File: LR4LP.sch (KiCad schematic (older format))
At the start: 13 parts, among them U2 NE5532

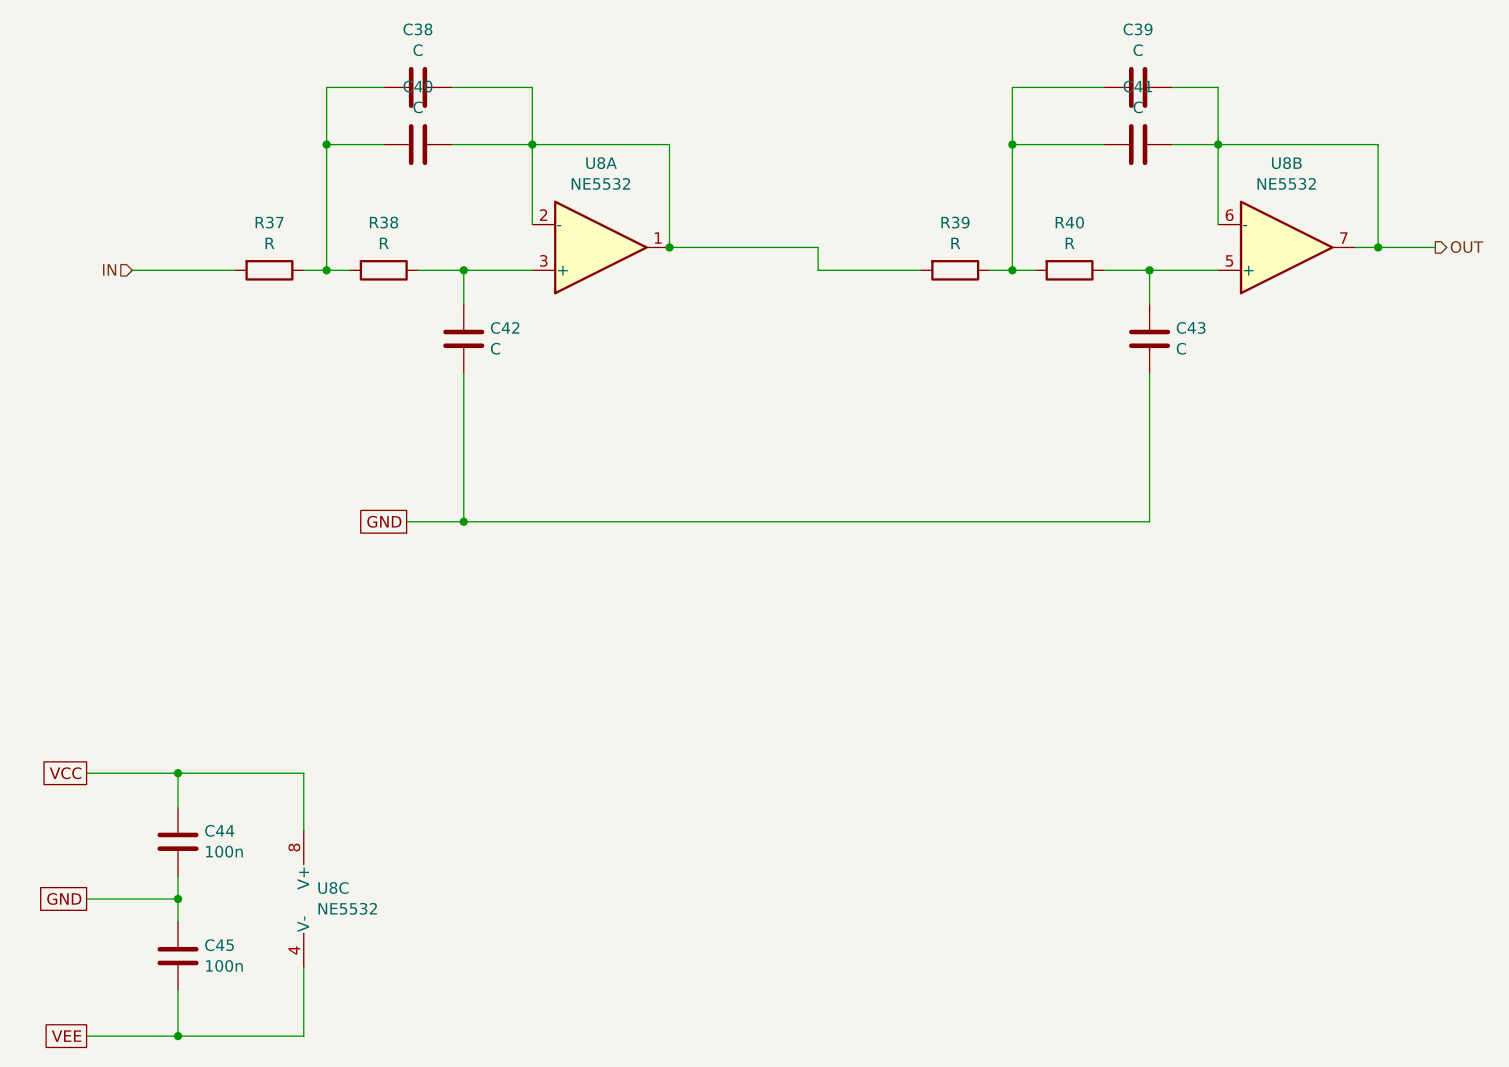
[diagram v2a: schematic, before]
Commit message: inverted LF processing chain, now with BW2 subsonic filter
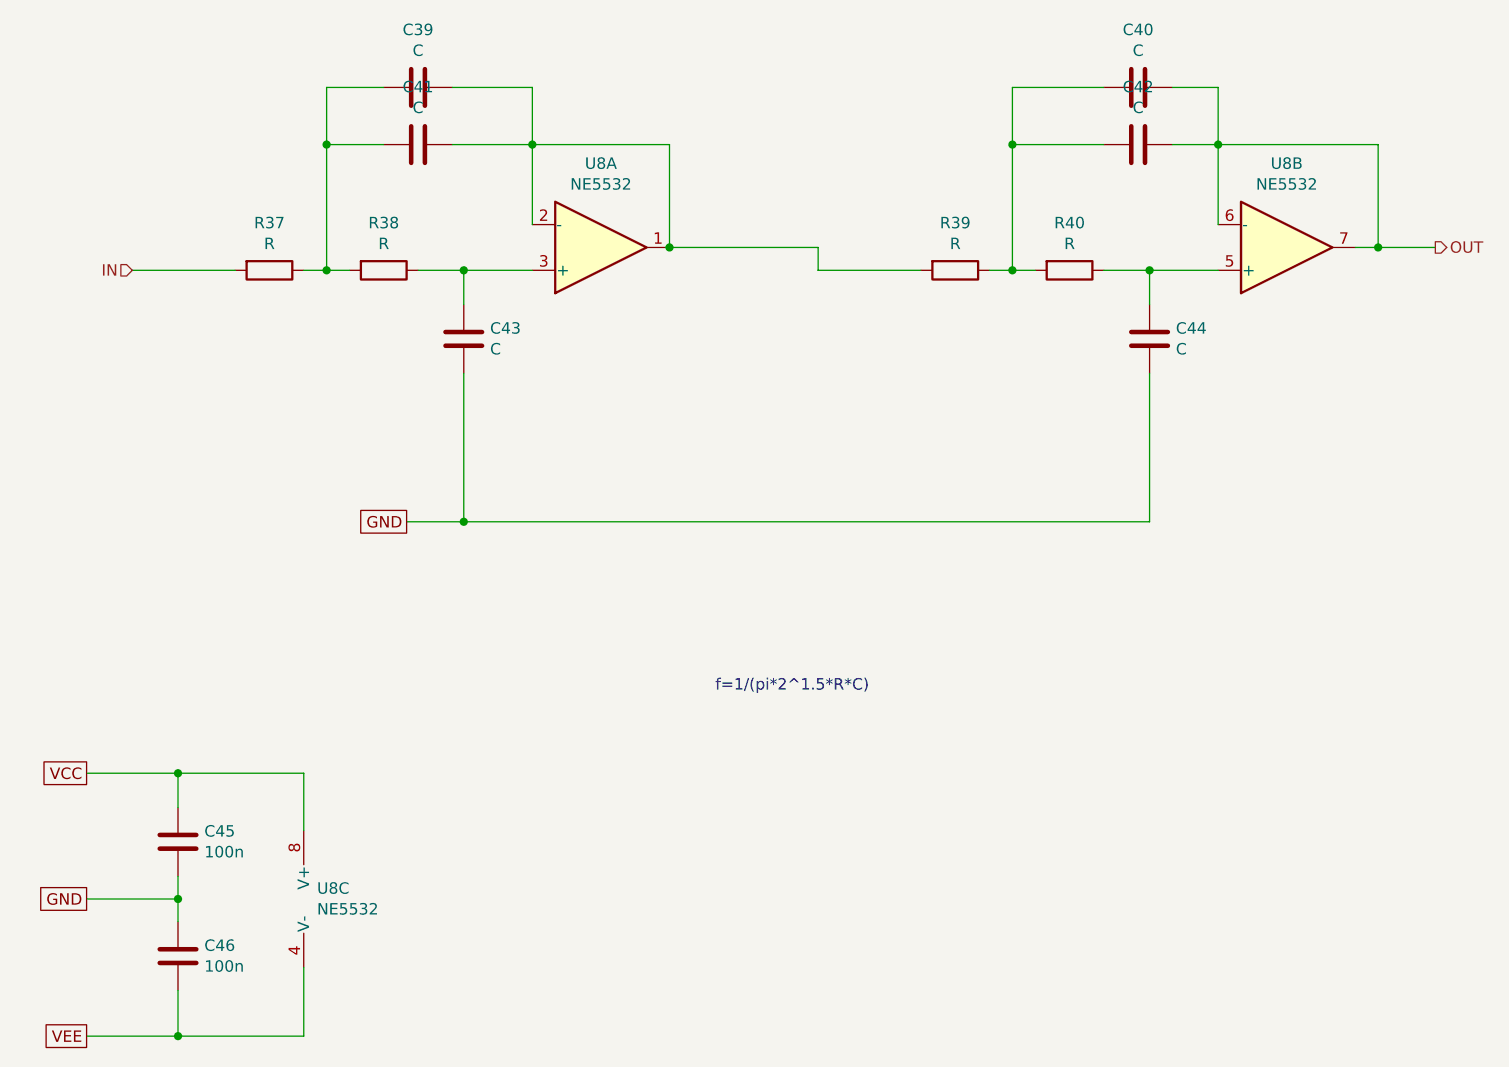
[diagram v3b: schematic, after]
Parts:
- renumbered C9 to C10, C10 to C11, C11 to C12, C4 to C5, C5 to C6, C6 to C7, C7 to C8, C8 to C9
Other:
- note added: "f=1/(pi*2^1.5*R*C)"
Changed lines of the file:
@@
 $Descr A4 11693 8268
 encoding utf-8
-Sheet 7 19
+Sheet 7 17
 Title "4th Order Linkwitz-Riley Low-Pass"
 Date "2021-10-03"
@@
 P 3000 5450
 AR Path="/6157B871/615EA97C" Ref="C?"  Part="1"
-AR Path="/615E7263/615EA97C" Ref="C11"  Part="1"
-AR Path="/615961F5/615EA97C" Ref="C25"  Part="1"
+AR Path="/615E7263/615EA97C" Ref="C12"  Part="1"
+AR Path="/615961F5/615EA97C" Ref="C26"  Part="1"
 AR Path="/61596D2E/615EA97C" Ref="C?"  Part="1"
 AR Path="/61597705/615EA97C" Ref="C?"  Part="1"
-AR Path="/615C4B58/615EA97C" Ref="C45"  Part="1"
-F 0 "C45" H 3115 5496 50  0000 L CNN
+AR Path="/615C4B58/615EA97C" Ref="C46"  Part="1"
+F 0 "C46" H 3115 5496 50  0000 L CNN
 F 1 "100n" H 3115 5405 50  0000 L CNN
 F 2 "Capacitors_SMD:C_0805" H 3038 5300 50  0001 C CNN
@@
 P 4050 1900
 AR Path="/6157B871/615EA9A2" Ref="C?"  Part="1"
-AR Path="/615E7263/615EA9A2" Ref="C6"  Part="1"
-AR Path="/615961F5/615EA9A2" Ref="C20"  Part="1"
+AR Path="/615E7263/615EA9A2" Ref="C7"  Part="1"
+AR Path="/615961F5/615EA9A2" Ref="C21"  Part="1"
 AR Path="/61596D2E/615EA9A2" Ref="C?"  Part="1"
 AR Path="/61597705/615EA9A2" Ref="C?"  Part="1"
-AR Path="/615C4B58/615EA9A2" Ref="C40"  Part="1"
-F 0 "C40" V 3798 1900 50  0000 C CNN
+AR Path="/615C4B58/615EA9A2" Ref="C41"  Part="1"
+F 0 "C41" V 3798 1900 50  0000 C CNN
 F 1 "C" V 3889 1900 50  0000 C CNN
 F 2 "Capacitors_SMD:C_1210_HandSoldering" H 4088 1750 50  0001 C CNN
@@
 P 4250 2750
 AR Path="/6157B871/615EA9A8" Ref="C?"  Part="1"
-AR Path="/615E7263/615EA9A8" Ref="C8"  Part="1"
-AR Path="/615961F5/615EA9A8" Ref="C22"  Part="1"
+AR Path="/615E7263/615EA9A8" Ref="C9"  Part="1"
+AR Path="/615961F5/615EA9A8" Ref="C23"  Part="1"
 AR Path="/61596D2E/615EA9A8" Ref="C?"  Part="1"
 AR Path="/61597705/615EA9A8" Ref="C?"  Part="1"
-AR Path="/615C4B58/615EA9A8" Ref="C42"  Part="1"
-F 0 "C42" H 4135 2704 50  0000 R CNN
+AR Path="/615C4B58/615EA9A8" Ref="C43"  Part="1"
+F 0 "C43" H 4135 2704 50  0000 R CNN
 F 1 "C" H 4135 2795 50  0000 R CNN
 F 2 "Capacitors_SMD:C_1210_HandSoldering" H 4288 2600 50  0001 C CNN
@@
 P 3000 4950
 AR Path="/6157B871/615EA9EC" Ref="C?"  Part="1"
-AR Path="/615E7263/615EA9EC" Ref="C10"  Part="1"
-AR Path="/615961F5/615EA9EC" Ref="C24"  Part="1"
+AR Path="/615E7263/615EA9EC" Ref="C11"  Part="1"
+AR Path="/615961F5/615EA9EC" Ref="C25"  Part="1"
 AR Path="/61596D2E/615EA9EC" Ref="C?"  Part="1"
 AR Path="/61597705/615EA9EC" Ref="C?"  Part="1"
-AR Path="/615C4B58/615EA9EC" Ref="C44"  Part="1"
-F 0 "C44" H 3115 4996 50  0000 L CNN
+AR Path="/615C4B58/615EA9EC" Ref="C45"  Part="1"
+F 0 "C45" H 3115 4996 50  0000 L CNN
 F 1 "100n" H 3115 4905 50  0000 L CNN
 F 2 "Capacitors_SMD:C_0805" H 3038 4800 50  0001 C CNN
@@
 P 4050 1650
 AR Path="/6157B871/6160176B" Ref="C?"  Part="1"
-AR Path="/615E7263/6160176B" Ref="C4"  Part="1"
-AR Path="/615961F5/6160176B" Ref="C18"  Part="1"
+AR Path="/615E7263/6160176B" Ref="C5"  Part="1"
+AR Path="/615961F5/6160176B" Ref="C19"  Part="1"
 AR Path="/61596D2E/6160176B" Ref="C?"  Part="1"
 AR Path="/61597705/6160176B" Ref="C?"  Part="1"
-AR Path="/615C4B58/6160176B" Ref="C38"  Part="1"
-F 0 "C38" V 3798 1650 50  0000 C CNN
+AR Path="/615C4B58/6160176B" Ref="C39"  Part="1"
+F 0 "C39" V 3798 1650 50  0000 C CNN
 F 1 "C" V 3889 1650 50  0000 C CNN
 F 2 "Capacitors_SMD:C_1210_HandSoldering" H 4088 1500 50  0001 C CNN
@@
 P 7200 1900
 AR Path="/6157B871/61611E78" Ref="C?"  Part="1"
-AR Path="/615E7263/61611E78" Ref="C7"  Part="1"
-AR Path="/615961F5/61611E78" Ref="C21"  Part="1"
+AR Path="/615E7263/61611E78" Ref="C8"  Part="1"
+AR Path="/615961F5/61611E78" Ref="C22"  Part="1"
 AR Path="/61596D2E/61611E78" Ref="C?"  Part="1"
 AR Path="/61597705/61611E78" Ref="C?"  Part="1"
-AR Path="/615C4B58/61611E78" Ref="C41"  Part="1"
-F 0 "C41" V 6948 1900 50  0000 C CNN
+AR Path="/615C4B58/61611E78" Ref="C42"  Part="1"
+F 0 "C42" V 6948 1900 50  0000 C CNN
 F 1 "C" V 7039 1900 50  0000 C CNN
 F 2 "Capacitors_SMD:C_1210_HandSoldering" H 7238 1750 50  0001 C CNN
@@
 P 7250 2750
 AR Path="/6157B871/61611E7E" Ref="C?"  Part="1"
-AR Path="/615E7263/61611E7E" Ref="C9"  Part="1"
-AR Path="/615961F5/61611E7E" Ref="C23"  Part="1"
+AR Path="/615E7263/61611E7E" Ref="C10"  Part="1"
+AR Path="/615961F5/61611E7E" Ref="C24"  Part="1"
 AR Path="/61596D2E/61611E7E" Ref="C?"  Part="1"
 AR Path="/61597705/61611E7E" Ref="C?"  Part="1"
-AR Path="/615C4B58/61611E7E" Ref="C43"  Part="1"
-F 0 "C43" H 7135 2704 50  0000 R CNN
+AR Path="/615C4B58/61611E7E" Ref="C44"  Part="1"
+F 0 "C44" H 7135 2704 50  0000 R CNN
 F 1 "C" H 7135 2795 50  0000 R CNN
 F 2 "Capacitors_SMD:C_1210_HandSoldering" H 7288 2600 50  0001 C CNN
@@
 P 7200 1650
 AR Path="/6157B871/61611E88" Ref="C?"  Part="1"
-AR Path="/615E7263/61611E88" Ref="C5"  Part="1"
-AR Path="/615961F5/61611E88" Ref="C19"  Part="1"
+AR Path="/615E7263/61611E88" Ref="C6"  Part="1"
+AR Path="/615961F5/61611E88" Ref="C20"  Part="1"
 AR Path="/61596D2E/61611E88" Ref="C?"  Part="1"
 AR Path="/61597705/61611E88" Ref="C?"  Part="1"
-AR Path="/615C4B58/61611E88" Ref="C39"  Part="1"
-F 0 "C39" V 6948 1650 50  0000 C CNN
+AR Path="/615C4B58/61611E88" Ref="C40"  Part="1"
+F 0 "C40" V 6948 1650 50  0000 C CNN
 F 1 "C" V 7039 1650 50  0000 C CNN
 F 2 "Capacitors_SMD:C_1210_HandSoldering" H 7238 1500 50  0001 C CNN
@@
 Wire Wire Line
 	8250 2350 8500 2350
+Text Notes 5350 4300 0    50   ~ 0
+f=1/(pi*2^1.5*R*C)
 $EndSCHEMATC

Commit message: Board is placed and about half-routed
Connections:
- net VP1: now reaches C9.2, R6.1, U2.3 (+)
- net FB1: now reaches C5.1, C7.1, R7.2, U2.1, U2.2 (-)
- net VP2: now reaches C10.2, R8.1, U2.5 (+)
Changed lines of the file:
@@
 $Descr A4 11693 8268
 encoding utf-8
-Sheet 7 17
+Sheet 4 17
 Title "4th Order Linkwitz-Riley Low-Pass"
 Date "2021-10-03"
@@
 Wire Wire Line
 	8250 2350 8500 2350
-Text Notes 5350 4300 0    50   ~ 0
+Text Notes 5400 3000 0    50   ~ 0
 f=1/(pi*2^1.5*R*C)
+Text Label 3000 2450 0    50   ~ 0
+IN
+Text Label 4150 2450 0    50   ~ 0
+VP1
+Text Label 4800 1900 0    50   ~ 0
+FB1
+Text Label 7100 2450 0    50   ~ 0
+VP2
+Text Label 7800 1900 0    50   ~ 0
+FB2
 $EndSCHEMATC
